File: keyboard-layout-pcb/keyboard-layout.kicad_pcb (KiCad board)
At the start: 2 copper layers, 50 x 196.7 mm, 33 parts, among them J1 Conn_01x06, J2 Conn_01x02, J3 Conn_01x02, Q1 IRLB871, U1 TSOP384xx, U2 TSMP58000, U3 RFM9xLoRa

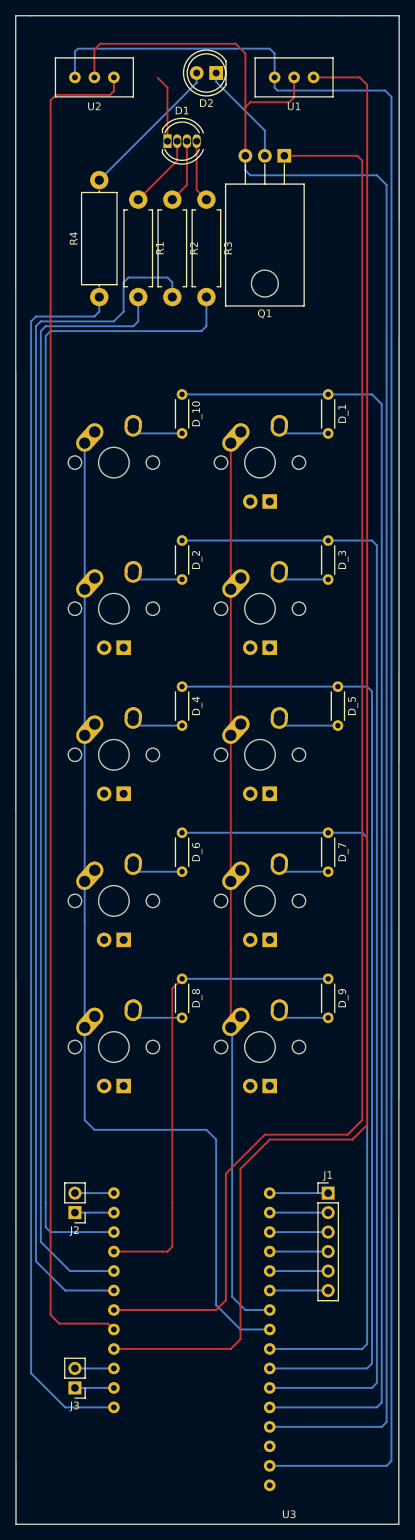
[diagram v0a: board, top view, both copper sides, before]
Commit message: Revert "Updated scematic to releft current operation"
This reverts commit bc39922ebd05a59e5cfd160ddaddfcfa669e5cef.
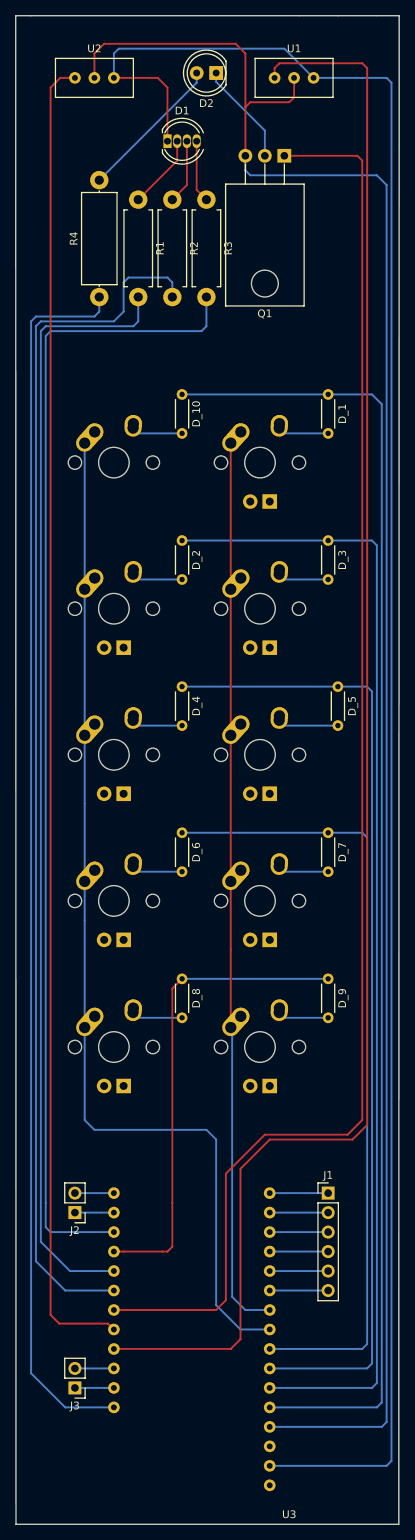
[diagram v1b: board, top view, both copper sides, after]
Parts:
- moved U1 5.02 mm to (74.3, 75.6), turned to 0 degrees
- moved U2 5.02 mm to (48.3, 75.6), turned to 0 degrees
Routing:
- net pin13: track 201.2 -> 209.8 mm
- net pin12: track 177.9 -> 172.8 mm
- net 3V: track 253.2 -> 252.2 mm
- net +5V: track 245.5 -> 244.6 mm
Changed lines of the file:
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@@
     (thickness 1.6)
     (drawings 27)
-    (tracks 191)
+    (tracks 190)
     (zones 0)
     (modules 33)
@@
   )
   (module Capstone:TSOP384 (layer F.Cu)
-    (at 48.26 80.5815 180)
-    (fp_text reference U2 (at 0 -1.27) (layer F.SilkS)
-      (effects (font (size 1 1) (thickness 0.15)))
-    )
-    (fp_text value TSMP58000 (at 0 -2.54) (layer F.Fab)
+    (at 74.295 75.565)
+    (fp_text reference U1 (at 0 -1.27) (layer F.SilkS)
+      (effects (font (size 1 1) (thickness 0.15)))
+    )
+    (fp_text value TSOP384xx (at 0 -2.54) (layer F.Fab)
       (effects (font (size 1 1) (thickness 0.15)))
     )
@@
     (fp_line (start 5.08 5.08) (end 5.08 0) (layer F.SilkS) (width 0.15))
     (fp_line (start 5.08 0) (end -5.08 0) (layer F.SilkS) (width 0.15))
-    (pad 1 thru_hole circle (at -2.54 2.54 180) (size 1.524 1.524) (drill 0.762) (layers *.Cu *.Mask)
-      (net 28 pin12))
-    (pad 2 thru_hole circle (at 0 2.54 180) (size 1.524 1.524) (drill 0.762) (layers *.Cu *.Mask)
+    (pad 1 thru_hole circle (at -2.54 2.54) (size 1.524 1.524) (drill 0.762) (layers *.Cu *.Mask)
+      (net 31 pin13))
+    (pad 2 thru_hole circle (at 0 2.54) (size 1.524 1.524) (drill 0.762) (layers *.Cu *.Mask)
       (net 42 +5V))
-    (pad 3 thru_hole circle (at 2.54 2.54 180) (size 1.524 1.524) (drill 0.762) (layers *.Cu *.Mask)
+    (pad 3 thru_hole circle (at 2.54 2.54) (size 1.524 1.524) (drill 0.762) (layers *.Cu *.Mask)
       (net 43 3V))
   )
   (module Capstone:TSOP384 (layer F.Cu)
-    (at 74.295 80.5815 180)
-    (fp_text reference U1 (at 0 -1.27) (layer F.SilkS)
-      (effects (font (size 1 1) (thickness 0.15)))
-    )
-    (fp_text value TSOP384xx (at 0 -2.54) (layer F.Fab)
+    (at 48.26 75.565)
+    (fp_text reference U2 (at 0 -1.27) (layer F.SilkS)
+      (effects (font (size 1 1) (thickness 0.15)))
+    )
+    (fp_text value TSMP58000 (at 0 -2.54) (layer F.Fab)
       (effects (font (size 1 1) (thickness 0.15)))
     )
@@
     (fp_line (start 5.08 5.08) (end 5.08 0) (layer F.SilkS) (width 0.15))
     (fp_line (start 5.08 0) (end -5.08 0) (layer F.SilkS) (width 0.15))
-    (pad 1 thru_hole circle (at -2.54 2.54 180) (size 1.524 1.524) (drill 0.762) (layers *.Cu *.Mask)
-      (net 31 pin13))
-    (pad 2 thru_hole circle (at 0 2.54 180) (size 1.524 1.524) (drill 0.762) (layers *.Cu *.Mask)
+    (pad 1 thru_hole circle (at -2.54 2.54) (size 1.524 1.524) (drill 0.762) (layers *.Cu *.Mask)
+      (net 28 pin12))
+    (pad 2 thru_hole circle (at 0 2.54) (size 1.524 1.524) (drill 0.762) (layers *.Cu *.Mask)
       (net 42 +5V))
-    (pad 3 thru_hole circle (at 2.54 2.54 180) (size 1.524 1.524) (drill 0.762) (layers *.Cu *.Mask)
+    (pad 3 thru_hole circle (at 2.54 2.54) (size 1.524 1.524) (drill 0.762) (layers *.Cu *.Mask)
       (net 43 3V))
   )
@@
   (segment (start 41.91 227.965) (end 42.545 228.6) (width 0.25) (layer B.Cu) (net 27))
   (segment (start 42.545 228.6) (end 45.72 228.6) (width 0.25) (layer B.Cu) (net 27))
-  (segment (start 50.8 79.8195) (end 50.8 78.0415) (width 0.25) (layer F.Cu) (net 28))
   (segment (start 50.038001 240.538001) (end 43.688001 240.538001) (width 0.25) (layer F.Cu) (net 28))
-  (segment (start 50.8 241.3) (end 50.038001 240.538001) (width 0.25) (layer F.Cu) (net 28))
+  (segment (start 50.8 241.3) (end 50.038001 240.538001) (width 0.25) (layer F.Cu) (net 28) (status 10))
   (segment (start 43.688001 240.538001) (end 42.545 239.395) (width 0.25) (layer F.Cu) (net 28))
-  (segment (start 50.292 80.3275) (end 50.8 79.8195) (width 0.25) (layer F.Cu) (net 28))
-  (segment (start 42.545 239.395) (end 42.545 81.026) (width 0.25) (layer F.Cu) (net 28))
-  (segment (start 42.545 81.026) (end 43.2435 80.3275) (width 0.25) (layer F.Cu) (net 28))
-  (segment (start 43.2435 80.3275) (end 50.292 80.3275) (width 0.25) (layer F.Cu) (net 28))
-  (segment (start 82.8675 78.0415) (end 76.835 78.0415) (width 0.25) (layer F.Cu) (net 31))
-  (segment (start 83.82 214.63) (end 83.82 78.994) (width 0.25) (layer F.Cu) (net 31))
+  (segment (start 42.545 239.395) (end 42.545 79.375) (width 0.25) (layer F.Cu) (net 28))
+  (segment (start 42.545 79.375) (end 43.815 78.105) (width 0.25) (layer F.Cu) (net 28))
+  (segment (start 43.815 78.105) (end 45.72 78.105) (width 0.25) (layer F.Cu) (net 28))
+  (segment (start 71.755 76.835) (end 71.755 78.105) (width 0.25) (layer F.Cu) (net 31))
+  (segment (start 83.185 76.2) (end 72.39 76.2) (width 0.25) (layer F.Cu) (net 31))
+  (segment (start 83.82 214.63) (end 83.82 76.835) (width 0.25) (layer F.Cu) (net 31))
+  (segment (start 66.04 243.84) (end 67.31 242.57) (width 0.25) (layer F.Cu) (net 31))
+  (segment (start 83.82 76.835) (end 83.185 76.2) (width 0.25) (layer F.Cu) (net 31))
   (segment (start 50.8 243.84) (end 66.04 243.84) (width 0.25) (layer F.Cu) (net 31))
   (segment (start 67.31 242.57) (end 67.31 220.345) (width 0.25) (layer F.Cu) (net 31))
+  (segment (start 72.39 76.2) (end 71.755 76.835) (width 0.25) (layer F.Cu) (net 31))
   (segment (start 67.31 220.345) (end 71.12 216.535) (width 0.25) (layer F.Cu) (net 31))
-  (segment (start 66.04 243.84) (end 67.31 242.57) (width 0.25) (layer F.Cu) (net 31))
   (segment (start 71.12 216.535) (end 81.915 216.535) (width 0.25) (layer F.Cu) (net 31))
-  (segment (start 83.82 78.994) (end 82.8675 78.0415) (width 0.25) (layer F.Cu) (net 31))
   (segment (start 81.915 216.535) (end 83.82 214.63) (width 0.25) (layer F.Cu) (net 31))
   (segment (start 71.12 223.52) (end 78.74 223.52) (width 0.25) (layer B.Cu) (net 32))
@@
   (segment (start 67.945 81.915) (end 67.945 88.265) (width 0.25) (layer F.Cu) (net 42) (status 20))
   (segment (start 67.945 81.915) (end 68.58 81.28) (width 0.25) (layer F.Cu) (net 42))
+  (segment (start 68.58 81.28) (end 73.66 81.28) (width 0.25) (layer F.Cu) (net 42))
+  (segment (start 73.66 81.28) (end 74.295 80.645) (width 0.25) (layer F.Cu) (net 42))
+  (segment (start 74.295 80.645) (end 74.295 78.105) (width 0.25) (layer F.Cu) (net 42))
   (segment (start 48.26 77.47) (end 48.26 78.105) (width 0.25) (layer F.Cu) (net 42))
-  (segment (start 68.58 81.28) (end 73.66 81.28) (width 0.25) (layer F.Cu) (net 42))
-  (segment (start 74.295 80.645) (end 74.295 78.0415) (width 0.25) (layer F.Cu) (net 42))
-  (segment (start 73.66 81.28) (end 74.295 80.645) (width 0.25) (layer F.Cu) (net 42))
-  (segment (start 48.26 74.422) (end 48.26 78.0415) (width 0.25) (layer F.Cu) (net 42))
-  (segment (start 49.022 73.66) (end 48.26 74.422) (width 0.25) (layer F.Cu) (net 42))
-  (segment (start 66.675 73.66) (end 49.022 73.66) (width 0.25) (layer F.Cu) (net 42))
+  (segment (start 48.26 74.93) (end 48.26 77.47) (width 0.25) (layer F.Cu) (net 42))
+  (segment (start 49.53 73.66) (end 48.26 74.93) (width 0.25) (layer F.Cu) (net 42))
+  (segment (start 66.675 73.66) (end 49.53 73.66) (width 0.25) (layer F.Cu) (net 42))
   (segment (start 67.945 81.915) (end 67.945 74.93) (width 0.25) (layer F.Cu) (net 42))
   (segment (start 67.945 74.93) (end 66.675 73.66) (width 0.25) (layer F.Cu) (net 42))
   (segment (start 57.785 86.36) (end 57.785 86.725) (width 0.25) (layer F.Cu) (net 43) (status 30))
+  (segment (start 83.185 78.105) (end 76.835 78.105) (width 0.25) (layer B.Cu) (net 43))
+  (segment (start 86.36 78.105) (end 83.185 78.105) (width 0.25) (layer B.Cu) (net 43))
+  (segment (start 86.995 78.74) (end 86.36 78.105) (width 0.25) (layer B.Cu) (net 43))
+  (segment (start 86.995 258.445) (end 86.995 78.74) (width 0.25) (layer B.Cu) (net 43))
+  (segment (start 71.12 259.08) (end 86.36 259.08) (width 0.25) (layer B.Cu) (net 43))
+  (segment (start 86.36 259.08) (end 86.995 258.445) (width 0.25) (layer B.Cu) (net 43))
+  (segment (start 76.835 78.105) (end 73.025 74.295) (width 0.25) (layer B.Cu) (net 43))
+  (segment (start 73.025 74.295) (end 51.435 74.295) (width 0.25) (layer B.Cu) (net 43))
+  (segment (start 51.435 74.295) (end 50.8 74.93) (width 0.25) (layer B.Cu) (net 43))
+  (segment (start 50.8 74.93) (end 50.8 78.105) (width 0.25) (layer B.Cu) (net 43))
   (segment (start 57.785 79.375) (end 57.785 86.36) (width 0.25) (layer F.Cu) (net 43))
+  (segment (start 50.8 78.105) (end 56.515 78.105) (width 0.25) (layer F.Cu) (net 43))
   (segment (start 56.515 78.105) (end 57.785 79.375) (width 0.25) (layer F.Cu) (net 43))
-  (segment (start 86.36 259.08) (end 86.995 258.445) (width 0.25) (layer B.Cu) (net 43))
-  (segment (start 71.12 259.08) (end 86.36 259.08) (width 0.25) (layer B.Cu) (net 43))
-  (segment (start 86.995 258.445) (end 86.995 80.5815) (width 0.25) (layer B.Cu) (net 43))
-  (segment (start 71.755 79.375) (end 71.755 78.0415) (width 0.25) (layer B.Cu) (net 43))
-  (segment (start 86.995 80.5815) (end 86.1695 79.756) (width 0.25) (layer B.Cu) (net 43))
-  (segment (start 86.1695 79.756) (end 72.136 79.756) (width 0.25) (layer B.Cu) (net 43))
-  (segment (start 72.136 79.756) (end 71.755 79.375) (width 0.25) (layer B.Cu) (net 43))
-  (segment (start 45.72 74.676) (end 45.72 78.0415) (width 0.25) (layer B.Cu) (net 43))
-  (segment (start 46.101 74.295) (end 45.72 74.676) (width 0.25) (layer B.Cu) (net 43))
-  (segment (start 71.12 74.295) (end 46.101 74.295) (width 0.25) (layer B.Cu) (net 43))
-  (segment (start 71.755 78.0415) (end 71.755 74.93) (width 0.25) (layer B.Cu) (net 43))
-  (segment (start 71.755 74.93) (end 71.12 74.295) (width 0.25) (layer B.Cu) (net 43))
 )
